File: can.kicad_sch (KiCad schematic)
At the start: 18 parts, among them U1 SN6501DBVR, U2 ISO1050DWR, U3 TPS76350DBVR

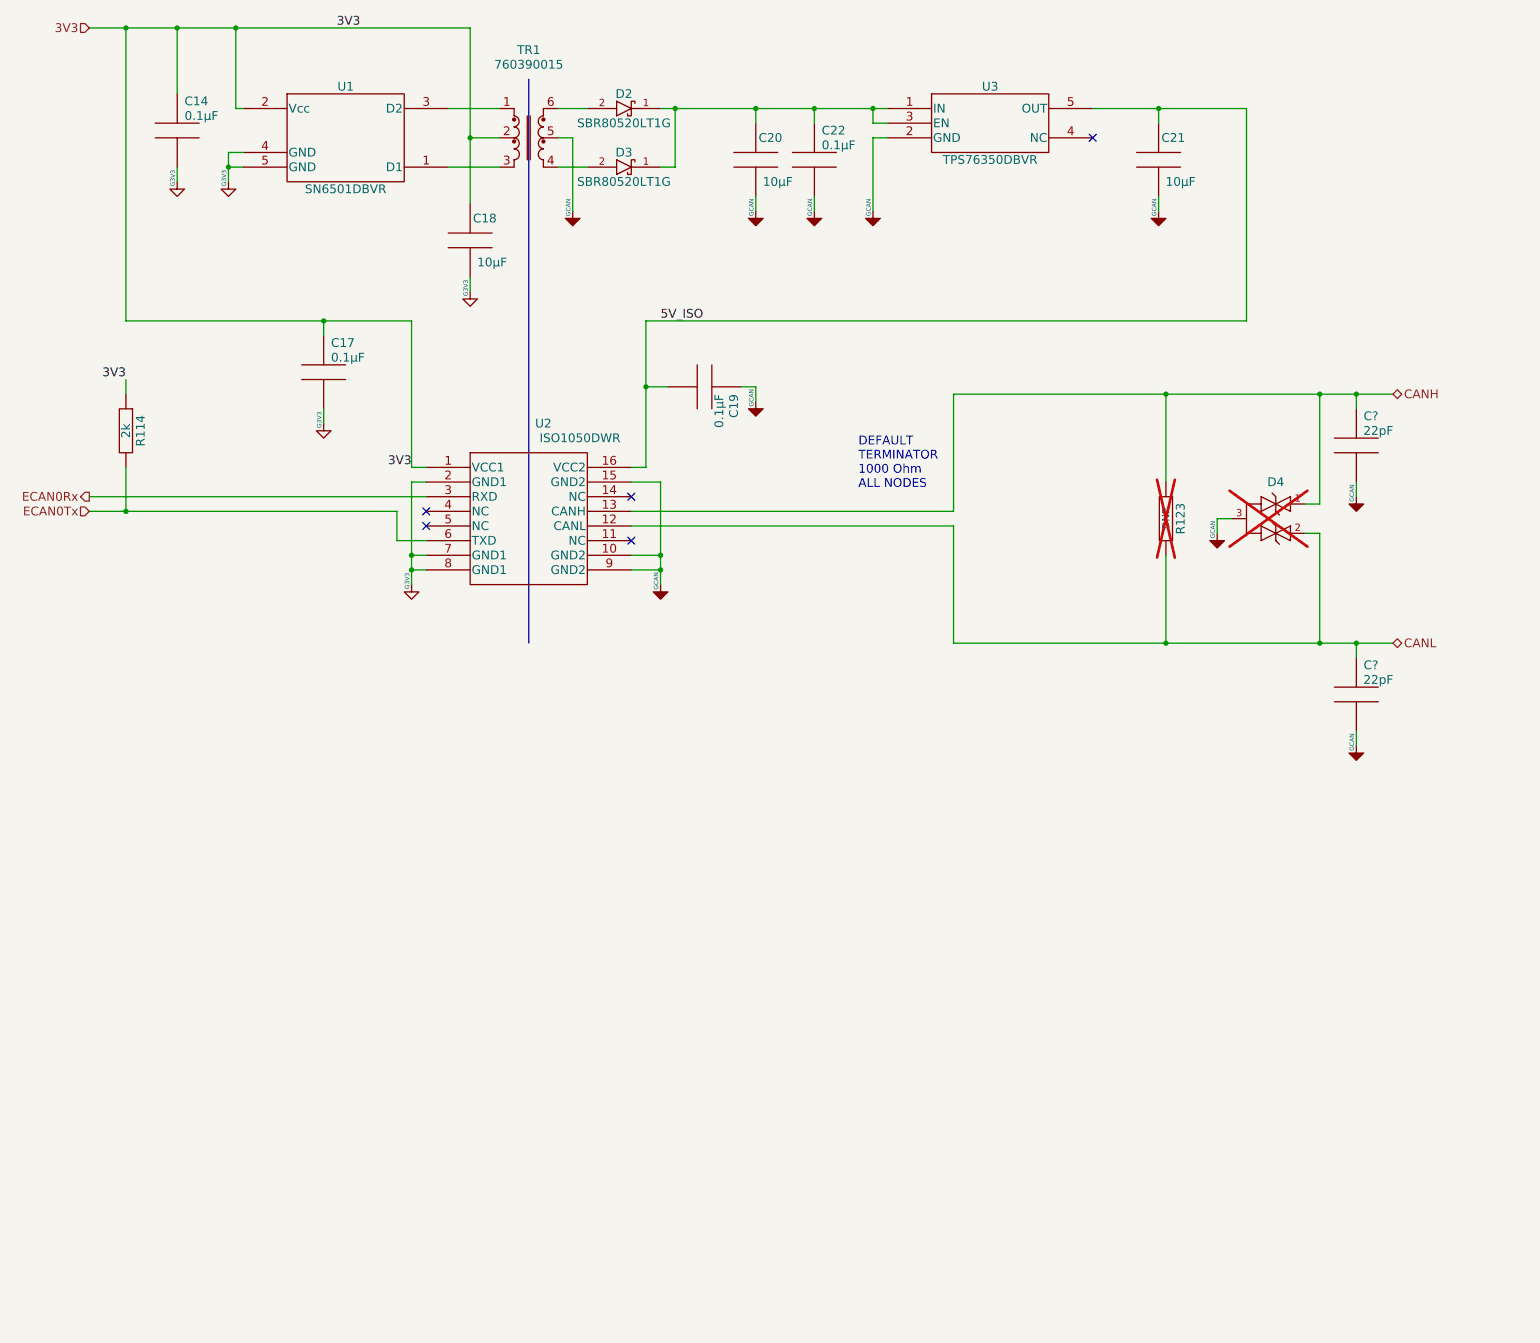
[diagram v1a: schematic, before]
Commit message: kicad 9 - r11-check gerber before sending to manufacturing
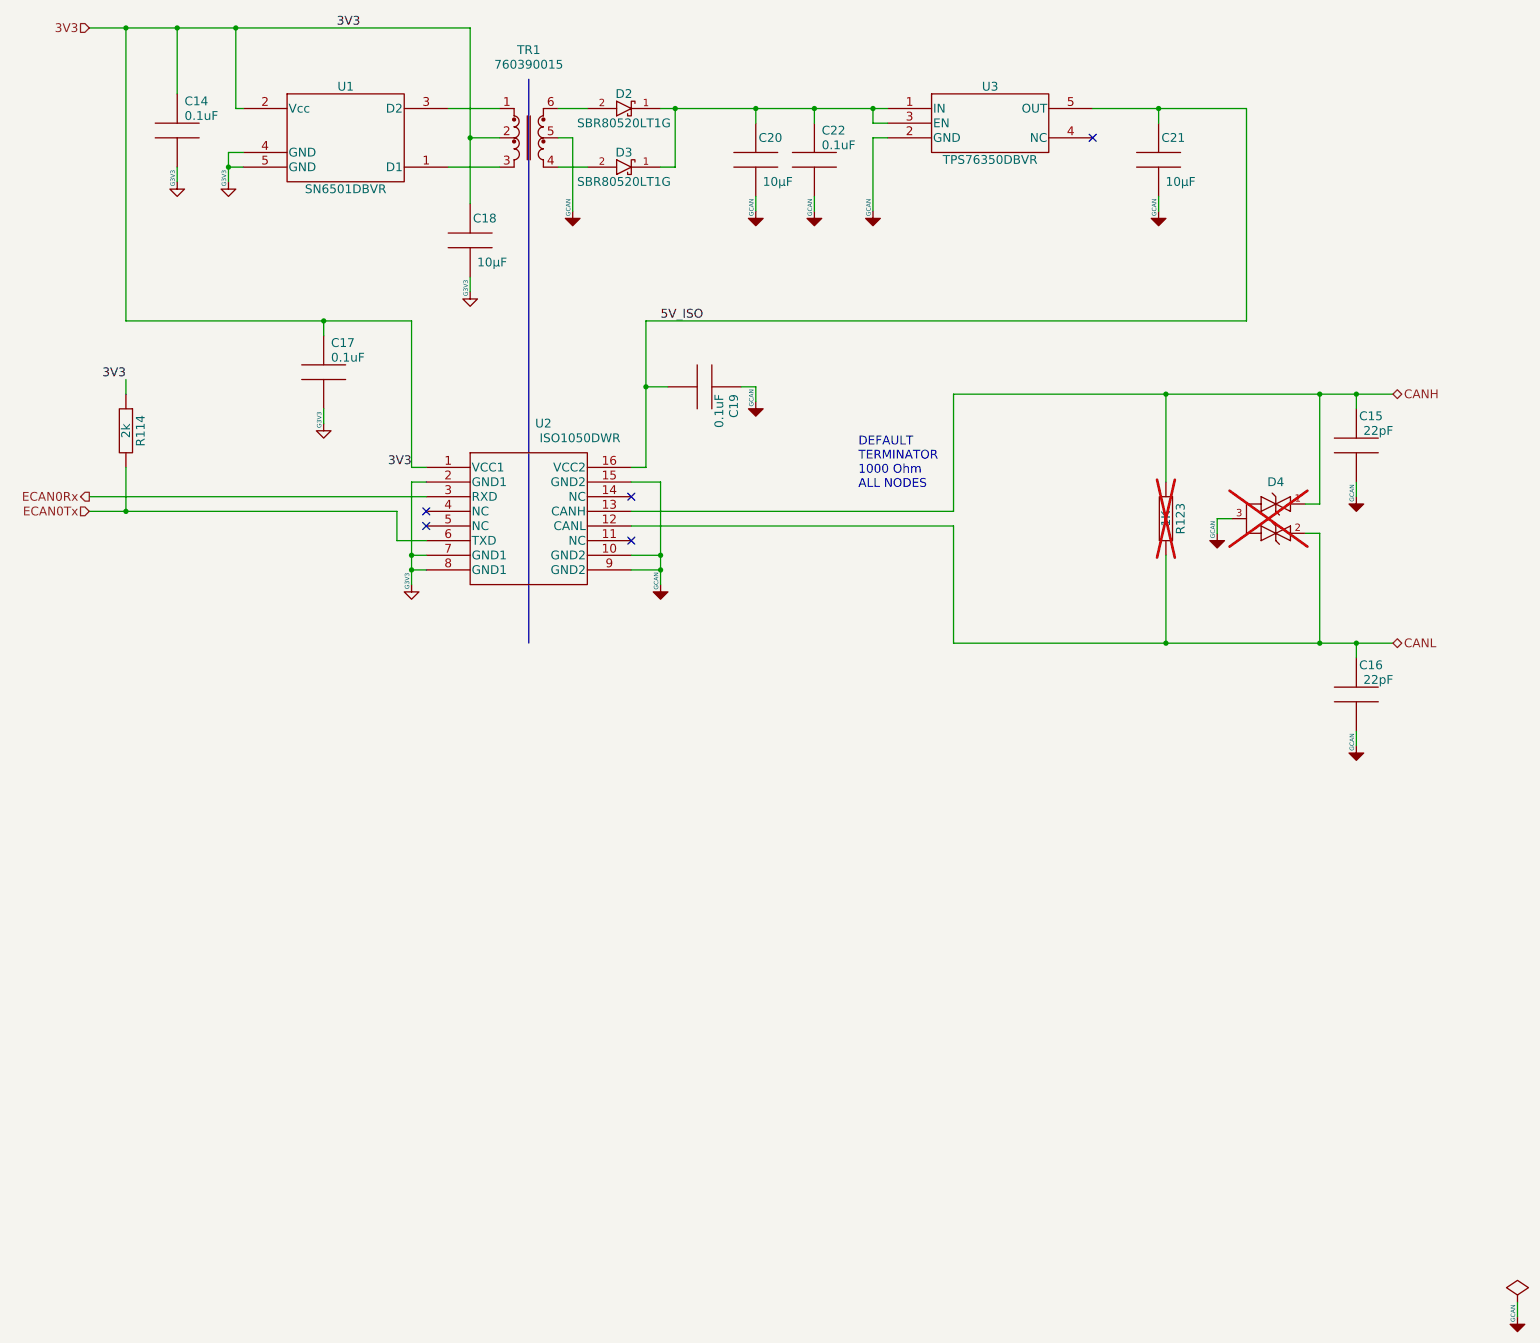
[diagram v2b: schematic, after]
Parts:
- C14, C17, C19, C22: Nominal 0.1µF -> 0.1uF; SupllierPartNumber 478-3352-1-ND -> (none)
- C18, C20, C21: SupllierPartNumber 478-5728-1-ND -> (none)
- D2, D3: SupllierPartNumber MBR0520LCT-ND -> (none)
- D4: SupllierPartNumber 497-17303-1-ND -> (none); fit_field DNP -> (none)
- R114: SupllierPartNumber 311-2.00KCRCT-ND -> (none)
- R123: SupllierPartNumber 311-1.00KCRCT-ND -> (none); Tolerance 1% -> (none); fit_field DNP -> (none)
- TR1: SupllierPartNumber 732-4459-1-ND -> (none)
- U1: SupllierPartNumber 296-37700-1-ND -> (none)
- U2: SupllierPartNumber 296-41267-1-ND -> (none)
- U3: SupllierPartNumber 296-11023-1-ND -> (none)
- gave numbers to parts that had none: 2
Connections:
- net GNDD renamed GND_3V3

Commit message: r11a - clean up mostly with reports naming, values, footprints and parts
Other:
- company: ARXTRON TECHNOLOGIES -> ${COMPANY}
- title: EOL ECU MIX CARD -> ${PART_NUM} ${PCB_NAME} ${ASSY_VARIANT} ${ASSY_NAME}
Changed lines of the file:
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@@
 	(paper "A3")
 	(title_block
-		(title "EOL ECU MIX CARD")
-		(date "2023-09-26")
-		(rev "0C")
-		(company "ARXTRON TECHNOLOGIES")
-		(comment 1 "A0180-V0")
-		(comment 2 "PRJ22180")
-		(comment 3 "EOL ECU RCM8 RCM9")
-		(comment 4 "ANTON TOKARSKYI")
+		(title "${PART_NUM} ${PCB_NAME} ${ASSY_VARIANT} ${ASSY_NAME}")
+		(date "2025-03-12")
+		(rev "${REVISION}${REVISION_SCH}")
+		(company "${COMPANY}")
+		(comment 1 "${PART_NUM}")
+		(comment 2 "${PRJ_NUM}")
+		(comment 3 "${PRJ_NAME}")
+		(comment 4 "${DESIGNED}")
+		(comment 5 "${PART_NUM_ICT}")
 	)
 	(text "DEFAULT\nTERMINATOR\n1000 Ohm\nALL NODES"
